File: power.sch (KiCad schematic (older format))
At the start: 19 parts, among them Q1 DMP6023LSS, U1 LMR16006

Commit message: Add 24V outputs.
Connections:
- net VIN renamed VIN+
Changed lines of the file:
@@
 Comment4 ""
 $EndDescr
-$Comp
-L VIN #PWR03
-U 1 1 562BB258
-P 750 1250
-F 0 "#PWR03" H 750 1100 50  0001 C CNN
-F 1 "VIN" H 750 1390 50  0000 C CNN
-F 2 "" H 750 1250 60  0000 C CNN
-F 3 "" H 750 1250 60  0000 C CNN
-	1    750  1250
-	1    0    0    -1
-$EndComp
 Text Notes 550  1000 0    60   ~ 0
 24 V
@@
 F 3 "" H 1200 2450 30  0000 C CNN
 	1    1200 2450
-	1    0    0    -1
-$EndComp
-$Comp
-L GND #PWR04
-U 1 1 5637DBF8
-P 1200 2900
-F 0 "#PWR04" H 1200 2650 50  0001 C CNN
-F 1 "GND" H 1200 2750 50  0000 C CNN
-F 2 "" H 1200 2900 60  0000 C CNN
-F 3 "" H 1200 2900 60  0000 C CNN
-	1    1200 2900
 	1    0    0    -1
 $EndComp
@@
 $EndComp
 $Comp
-L GND #PWR05
-U 1 1 57AF3EE9
-P 850 2900
-F 0 "#PWR05" H 850 2650 50  0001 C CNN
-F 1 "GND" H 850 2750 50  0000 C CNN
-F 2 "" H 850 2900 60  0000 C CNN
-F 3 "" H 850 2900 60  0000 C CNN
-	1    850  2900
-	1    0    0    -1
-$EndComp
-$Comp
-L GND #PWR06
+L GND #PWR013
 U 1 1 57C23EF3
 P 4100 5750
-F 0 "#PWR06" H 4100 5500 50  0001 C CNN
+F 0 "#PWR013" H 4100 5500 50  0001 C CNN
 F 1 "GND" H 4100 5600 50  0000 C CNN
 F 2 "" H 4100 5750 60  0000 C CNN
@@
 $EndComp
 $Comp
-L GNDA #PWR07
+L GNDA #PWR014
 U 1 1 57C23EF9
 P 4700 5750
-F 0 "#PWR07" H 4700 5500 50  0001 C CNN
+F 0 "#PWR014" H 4700 5500 50  0001 C CNN
 F 1 "GNDA" H 4700 5600 50  0000 C CNN
 F 2 "" H 4700 5750 60  0000 C CNN
@@
 $EndComp
 $Comp
-L +3.3V #PWR08
+L +3.3V #PWR015
 U 1 1 57C23F59
 P 4100 5450
-F 0 "#PWR08" H 4100 5300 50  0001 C CNN
+F 0 "#PWR015" H 4100 5300 50  0001 C CNN
 F 1 "+3.3V" H 4115 5623 50  0000 C CNN
 F 2 "" H 4100 5450 50  0000 C CNN
@@
 $EndComp
 $Comp
-L GND #PWR09
+L GND #PWR016
 U 1 1 57D426D3
 P 4150 2150
-F 0 "#PWR09" H 4150 1900 50  0001 C CNN
+F 0 "#PWR016" H 4150 1900 50  0001 C CNN
 F 1 "GND" H 4155 1977 50  0000 C CNN
 F 2 "" H 4150 2150 50  0000 C CNN
@@
 $EndComp
 $Comp
-L GND #PWR010
+L GND #PWR017
 U 1 1 57D42BF3
 P 4950 2400
-F 0 "#PWR010" H 4950 2150 50  0001 C CNN
+F 0 "#PWR017" H 4950 2150 50  0001 C CNN
 F 1 "GND" H 4955 2227 50  0000 C CNN
 F 2 "" H 4950 2400 50  0000 C CNN
@@
 $EndComp
 $Comp
-L GND #PWR011
+L GND #PWR018
 U 1 1 57D42C55
 P 5350 2400
-F 0 "#PWR011" H 5350 2150 50  0001 C CNN
+F 0 "#PWR018" H 5350 2150 50  0001 C CNN
 F 1 "GND" H 5355 2227 50  0000 C CNN
 F 2 "" H 5350 2400 50  0000 C CNN
@@
 $EndComp
 $Comp
-L GND #PWR012
+L GND #PWR019
 U 1 1 57D42CB7
 P 2900 2400
-F 0 "#PWR012" H 2900 2150 50  0001 C CNN
+F 0 "#PWR019" H 2900 2150 50  0001 C CNN
 F 1 "GND" H 2905 2227 50  0000 C CNN
 F 2 "" H 2900 2400 50  0000 C CNN
@@
 $EndComp
 $Comp
-L GND #PWR013
+L GND #PWR020
 U 1 1 57D42E3B
 P 2350 1850
-F 0 "#PWR013" H 2350 1600 50  0001 C CNN
+F 0 "#PWR020" H 2350 1600 50  0001 C CNN
 F 1 "GND" H 2355 1677 50  0000 C CNN
 F 2 "" H 2350 1850 50  0000 C CNN
@@
 $EndComp
 $Comp
-L +3.3V #PWR014
+L +3.3V #PWR021
 U 1 1 57D43B9E
 P 6350 1350
-F 0 "#PWR014" H 6350 1200 50  0001 C CNN
+F 0 "#PWR021" H 6350 1200 50  0001 C CNN
 F 1 "+3.3V" H 6365 1523 50  0000 C CNN
 F 2 "" H 6350 1350 50  0000 C CNN
@@
 $EndComp
 $Comp
-L +3.3VADC #PWR015
+L +3.3VADC #PWR022
 U 1 1 57C23F9D
 P 4700 5400
-F 0 "#PWR015" H 4850 5350 50  0001 C CNN
+F 0 "#PWR022" H 4850 5350 50  0001 C CNN
 F 1 "+3.3VADC" H 4720 5543 50  0000 C CNN
 F 2 "" H 4700 5400 50  0000 C CNN
@@
 Wire Wire Line
 	750  1250 750  1500
+$Comp
+L VIN+ #PWR023
+U 1 1 5870D4CB
+P 750 1250
+F 0 "#PWR023" H 750 1100 50  0001 C CNN
+F 1 "VIN+" H 765 1423 50  0000 C CNN
+F 2 "" H 750 1250 60  0000 C CNN
+F 3 "" H 750 1250 60  0000 C CNN
+	1    750  1250
+	1    0    0    -1
+$EndComp
+$Comp
+L GND #PWR024
+U 1 1 5637DBF8
+P 1200 2900
+F 0 "#PWR024" H 1200 2650 50  0001 C CNN
+F 1 "GND" H 1200 2750 50  0000 C CNN
+F 2 "" H 1200 2900 60  0000 C CNN
+F 3 "" H 1200 2900 60  0000 C CNN
+	1    1200 2900
+	1    0    0    -1
+$EndComp
+$Comp
+L GND #PWR025
+U 1 1 57AF3EE9
+P 850 2900
+F 0 "#PWR025" H 850 2650 50  0001 C CNN
+F 1 "GND" H 850 2750 50  0000 C CNN
+F 2 "" H 850 2900 60  0000 C CNN
+F 3 "" H 850 2900 60  0000 C CNN
+	1    850  2900
+	1    0    0    -1
+$EndComp
 $EndSCHEMATC

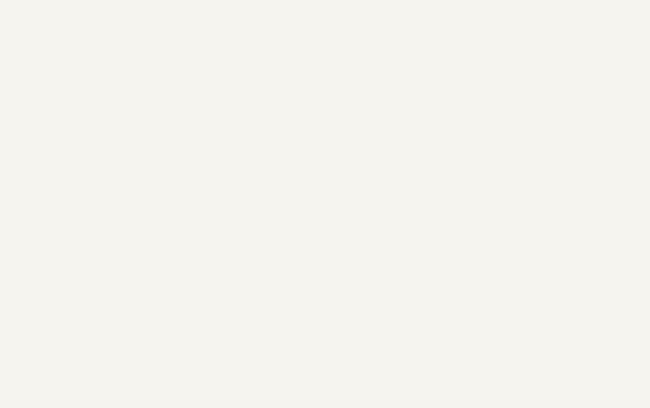
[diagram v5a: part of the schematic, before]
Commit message: Remove unnecessary 24V out, minor changes.
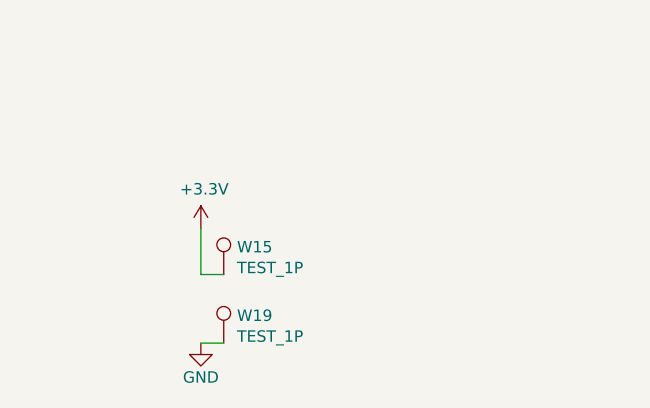
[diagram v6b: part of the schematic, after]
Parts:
- added W15, W19: TEST_1P, can-node:TH-Pad_1.5mm, symbol TEST_1P
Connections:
- net +3.3VADC: now also W15.1
- net GND: now also W19.1
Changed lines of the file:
@@
 $EndComp
 $Comp
-L GND #PWR013
+L GND #PWR03
 U 1 1 57C23EF3
 P 4100 5750
-F 0 "#PWR013" H 4100 5500 50  0001 C CNN
+F 0 "#PWR03" H 4100 5500 50  0001 C CNN
 F 1 "GND" H 4100 5600 50  0000 C CNN
 F 2 "" H 4100 5750 60  0000 C CNN
@@
 $EndComp
 $Comp
-L GNDA #PWR014
+L GNDA #PWR04
 U 1 1 57C23EF9
 P 4700 5750
-F 0 "#PWR014" H 4700 5500 50  0001 C CNN
+F 0 "#PWR04" H 4700 5500 50  0001 C CNN
 F 1 "GNDA" H 4700 5600 50  0000 C CNN
 F 2 "" H 4700 5750 60  0000 C CNN
@@
 $EndComp
 $Comp
-L +3.3V #PWR015
+L +3.3V #PWR05
 U 1 1 57C23F59
 P 4100 5450
-F 0 "#PWR015" H 4100 5300 50  0001 C CNN
+F 0 "#PWR05" H 4100 5300 50  0001 C CNN
 F 1 "+3.3V" H 4115 5623 50  0000 C CNN
 F 2 "" H 4100 5450 50  0000 C CNN
@@
 $EndComp
 $Comp
-L GND #PWR016
+L GND #PWR06
 U 1 1 57D426D3
 P 4150 2150
-F 0 "#PWR016" H 4150 1900 50  0001 C CNN
+F 0 "#PWR06" H 4150 1900 50  0001 C CNN
 F 1 "GND" H 4155 1977 50  0000 C CNN
 F 2 "" H 4150 2150 50  0000 C CNN
@@
 $EndComp
 $Comp
-L GND #PWR017
+L GND #PWR07
 U 1 1 57D42BF3
 P 4950 2400
-F 0 "#PWR017" H 4950 2150 50  0001 C CNN
+F 0 "#PWR07" H 4950 2150 50  0001 C CNN
 F 1 "GND" H 4955 2227 50  0000 C CNN
 F 2 "" H 4950 2400 50  0000 C CNN
@@
 $EndComp
 $Comp
-L GND #PWR018
+L GND #PWR08
 U 1 1 57D42C55
 P 5350 2400
-F 0 "#PWR018" H 5350 2150 50  0001 C CNN
+F 0 "#PWR08" H 5350 2150 50  0001 C CNN
 F 1 "GND" H 5355 2227 50  0000 C CNN
 F 2 "" H 5350 2400 50  0000 C CNN
@@
 $EndComp
 $Comp
-L GND #PWR019
+L GND #PWR09
 U 1 1 57D42CB7
 P 2900 2400
-F 0 "#PWR019" H 2900 2150 50  0001 C CNN
+F 0 "#PWR09" H 2900 2150 50  0001 C CNN
 F 1 "GND" H 2905 2227 50  0000 C CNN
 F 2 "" H 2900 2400 50  0000 C CNN
@@
 $EndComp
 $Comp
-L GND #PWR020
+L GND #PWR010
 U 1 1 57D42E3B
 P 2350 1850
-F 0 "#PWR020" H 2350 1600 50  0001 C CNN
+F 0 "#PWR010" H 2350 1600 50  0001 C CNN
 F 1 "GND" H 2355 1677 50  0000 C CNN
 F 2 "" H 2350 1850 50  0000 C CNN
@@
 $EndComp
 $Comp
-L +3.3V #PWR021
+L +3.3V #PWR011
 U 1 1 57D43B9E
 P 6350 1350
-F 0 "#PWR021" H 6350 1200 50  0001 C CNN
+F 0 "#PWR011" H 6350 1200 50  0001 C CNN
 F 1 "+3.3V" H 6365 1523 50  0000 C CNN
 F 2 "" H 6350 1350 50  0000 C CNN
@@
 $EndComp
 $Comp
-L +3.3VADC #PWR022
+L +3.3VADC #PWR012
 U 1 1 57C23F9D
 P 4700 5400
-F 0 "#PWR022" H 4850 5350 50  0001 C CNN
+F 0 "#PWR012" H 4850 5350 50  0001 C CNN
 F 1 "+3.3VADC" H 4720 5543 50  0000 C CNN
 F 2 "" H 4700 5400 50  0000 C CNN
@@
 	1    0    0    -1
 $EndComp
-Wire Wire Line
-	4100 5750 4700 5750
-Wire Wire Line
-	4100 5450 4700 5450
-Connection ~ 5800 1600
-Wire Wire Line
-	5800 1700 5800 1600
-Connection ~ 3800 2000
-Wire Wire Line
-	3800 2050 3800 2000
-Connection ~ 4150 1400
-Wire Wire Line
-	4250 1400 4250 1300
-Connection ~ 2850 1400
-Wire Wire Line
-	2850 1300 2850 1400
-Connection ~ 1900 1400
-Wire Wire Line
-	1900 1450 1900 1400
-Connection ~ 750  1400
-Connection ~ 2350 1400
-Wire Wire Line
-	2350 1500 2350 1400
-Wire Wire Line
-	2900 2400 2900 2000
-Connection ~ 5350 1600
-Wire Wire Line
-	6350 1600 6350 1350
-Wire Wire Line
-	5350 2400 5350 2050
-Connection ~ 4950 1600
-Wire Wire Line
-	5350 1600 5350 1750
-Connection ~ 4950 2000
-Wire Wire Line
-	3700 2000 4950 2000
-Wire Wire Line
-	4950 2400 4950 2350
-Wire Wire Line
-	4950 1950 4950 2050
-Wire Wire Line
-	4950 1600 4950 1650
-Wire Wire Line
-	4850 1600 6350 1600
-Wire Wire Line
-	2350 1800 2350 1850
-Connection ~ 2750 1400
-Wire Wire Line
-	2900 1700 2750 1700
-Connection ~ 4150 1600
-Wire Wire Line
-	4150 2150 4150 1950
-Wire Wire Line
-	3700 1600 4250 1600
-Wire Wire Line
-	4150 1400 4150 1650
-Wire Wire Line
-	4100 1400 4250 1400
-Wire Wire Line
-	3700 1400 3800 1400
-Wire Wire Line
-	4700 5450 4700 5400
-Wire Wire Line
-	1350 1400 2900 1400
-Wire Wire Line
-	850  2900 850  2500
-Connection ~ 850  1400
-Wire Wire Line
-	850  1900 850  1400
-Wire Wire Line
-	750  1400 950  1400
-Connection ~ 1600 1400
-Connection ~ 1200 2050
-Wire Wire Line
-	1600 2050 1200 2050
-Wire Wire Line
-	1200 1700 1200 2300
-Wire Wire Line
-	1600 1950 1600 2050
-Wire Wire Line
-	1600 1550 1600 1400
-Wire Wire Line
-	1200 2900 1200 2600
-Wire Wire Line
-	750  1250 750  1500
-$Comp
-L VIN+ #PWR023
+$Comp
+L VIN+ #PWR013
 U 1 1 5870D4CB
 P 750 1250
-F 0 "#PWR023" H 750 1100 50  0001 C CNN
+F 0 "#PWR013" H 750 1100 50  0001 C CNN
 F 1 "VIN+" H 765 1423 50  0000 C CNN
 F 2 "" H 750 1250 60  0000 C CNN
@@
 $EndComp
 $Comp
-L GND #PWR024
+L GND #PWR014
 U 1 1 5637DBF8
 P 1200 2900
-F 0 "#PWR024" H 1200 2650 50  0001 C CNN
+F 0 "#PWR014" H 1200 2650 50  0001 C CNN
 F 1 "GND" H 1200 2750 50  0000 C CNN
 F 2 "" H 1200 2900 60  0000 C CNN
@@
 $EndComp
 $Comp
-L GND #PWR025
+L GND #PWR015
 U 1 1 57AF3EE9
 P 850 2900
-F 0 "#PWR025" H 850 2650 50  0001 C CNN
+F 0 "#PWR015" H 850 2650 50  0001 C CNN
 F 1 "GND" H 850 2750 50  0000 C CNN
 F 2 "" H 850 2900 60  0000 C CNN
@@
 	1    0    0    -1
 $EndComp
+$Comp
+L TEST_1P W19
+U 1 1 58761A7C
+P 1450 6600
+F 0 "W19" H 1508 6720 50  0000 L CNN
+F 1 "TEST_1P" H 1508 6629 50  0000 L CNN
+F 2 "can-node:TH-Pad_1.5mm" H 1650 6600 50  0001 C CNN
+F 3 "" H 1650 6600 50  0000 C CNN
+	1    1450 6600
+	1    0    0    -1
+$EndComp
+$Comp
+L TEST_1P W15
+U 1 1 5876366A
+P 1450 6300
+F 0 "W15" H 1508 6420 50  0000 L CNN
+F 1 "TEST_1P" H 1508 6329 50  0000 L CNN
+F 2 "can-node:TH-Pad_1.5mm" H 1650 6300 50  0001 C CNN
+F 3 "" H 1650 6300 50  0000 C CNN
+	1    1450 6300
+	1    0    0    -1
+$EndComp
+$Comp
+L +3.3V #PWR017
+U 1 1 58763A3E
+P 1350 6100
+F 0 "#PWR017" H 1350 5950 50  0001 C CNN
+F 1 "+3.3V" H 1365 6273 50  0000 C CNN
+F 2 "" H 1350 6100 50  0000 C CNN
+F 3 "" H 1350 6100 50  0000 C CNN
+	1    1350 6100
+	1    0    0    -1
+$EndComp
+Wire Wire Line
+	4100 5750 4700 5750
+Wire Wire Line
+	4100 5450 4700 5450
+Connection ~ 5800 1600
+Wire Wire Line
+	5800 1700 5800 1600
+Connection ~ 3800 2000
+Wire Wire Line
+	3800 2050 3800 2000
+Connection ~ 4150 1400
+Wire Wire Line
+	4250 1400 4250 1300
+Connection ~ 2850 1400
+Wire Wire Line
+	2850 1300 2850 1400
+Connection ~ 1900 1400
+Wire Wire Line
+	1900 1450 1900 1400
+Connection ~ 750  1400
+Connection ~ 2350 1400
+Wire Wire Line
+	2350 1500 2350 1400
+Wire Wire Line
+	2900 2400 2900 2000
+Connection ~ 5350 1600
+Wire Wire Line
+	6350 1600 6350 1350
+Wire Wire Line
+	5350 2400 5350 2050
+Connection ~ 4950 1600
+Wire Wire Line
+	5350 1600 5350 1750
+Connection ~ 4950 2000
+Wire Wire Line
+	3700 2000 4950 2000
+Wire Wire Line
+	4950 2400 4950 2350
+Wire Wire Line
+	4950 1950 4950 2050
+Wire Wire Line
+	4950 1600 4950 1650
+Wire Wire Line
+	4850 1600 6350 1600
+Wire Wire Line
+	2350 1800 2350 1850
+Connection ~ 2750 1400
+Wire Wire Line
+	2900 1700 2750 1700
+Connection ~ 4150 1600
+Wire Wire Line
+	4150 2150 4150 1950
+Wire Wire Line
+	3700 1600 4250 1600
+Wire Wire Line
+	4150 1400 4150 1650
+Wire Wire Line
+	4100 1400 4250 1400
+Wire Wire Line
+	3700 1400 3800 1400
+Wire Wire Line
+	4700 5450 4700 5400
+Wire Wire Line
+	1350 1400 2900 1400
+Wire Wire Line
+	850  2900 850  2500
+Connection ~ 850  1400
+Wire Wire Line
+	850  1900 850  1400
+Wire Wire Line
+	750  1400 950  1400
+Connection ~ 1600 1400
+Connection ~ 1200 2050
+Wire Wire Line
+	1600 2050 1200 2050
+Wire Wire Line
+	1200 1700 1200 2300
+Wire Wire Line
+	1600 1950 1600 2050
+Wire Wire Line
+	1600 1550 1600 1400
+Wire Wire Line
+	1200 2900 1200 2600
+Wire Wire Line
+	750  1250 750  1500
+Wire Wire Line
+	1350 6100 1350 6300
+Wire Wire Line
+	1350 6300 1450 6300
+$Comp
+L GND #PWR?
+U 1 1 587684E1
+P 1350 6600
+F 0 "#PWR?" H 1350 6350 50  0001 C CNN
+F 1 "GND" H 1350 6450 50  0000 C CNN
+F 2 "" H 1350 6600 60  0000 C CNN
+F 3 "" H 1350 6600 60  0000 C CNN
+	1    1350 6600
+	1    0    0    -1
+$EndComp
+Wire Wire Line
+	1350 6600 1450 6600
 $EndSCHEMATC
